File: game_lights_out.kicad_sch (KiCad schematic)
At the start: 94 parts, among them SW1 SW_MEC_5E, SW10 SW_MEC_5E, SW11 SW_MEC_5E, SW12 SW_MEC_5E, SW13 SW_MEC_5E, SW14 SW_MEC_5E, SW15 SW_MEC_5E, SW16 SW_MEC_5E, SW17 SW_MEC_5E, SW18 SW_MEC_5E, SW19 SW_MEC_5E, SW2 SW_MEC_5E, SW20 SW_MEC_5E, SW21 SW_MEC_5E, SW22 SW_MEC_5E, SW23 SW_MEC_5E, SW24 SW_MEC_5E, SW25 SW_MEC_5E, SW26 SW_MEC_5E, SW27 SW_MEC_5E, SW28 SW_MEC_5E, SW29 SW_MEC_5E, SW3 SW_MEC_5E, SW30 SW_MEC_5E, SW31 SW_MEC_5E, SW32 SW_MEC_5E, SW33 SW_MEC_5E, SW34 SW_MEC_5E, SW35 SW_MEC_5E, SW36 SW_MEC_5E, SW37 SW_MEC_5E, SW38 SW_MEC_5E, SW39 SW_MEC_5E, SW4 SW_MEC_5E, SW40 SW_MEC_5E, SW5 SW_MEC_5E, SW6 SW_MEC_5E, SW7 SW_MEC_5E, SW8 SW_MEC_5E, SW9 SW_MEC_5E, U1 ATmega328-P, U2 ULN2803A

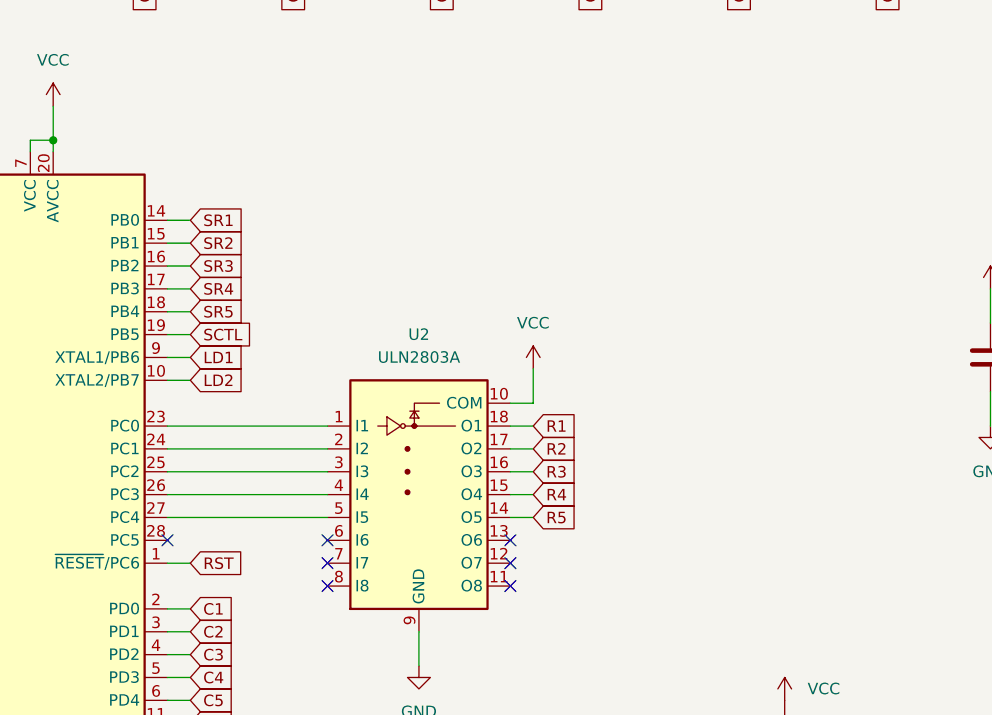
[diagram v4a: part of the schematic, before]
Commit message: Added speaker
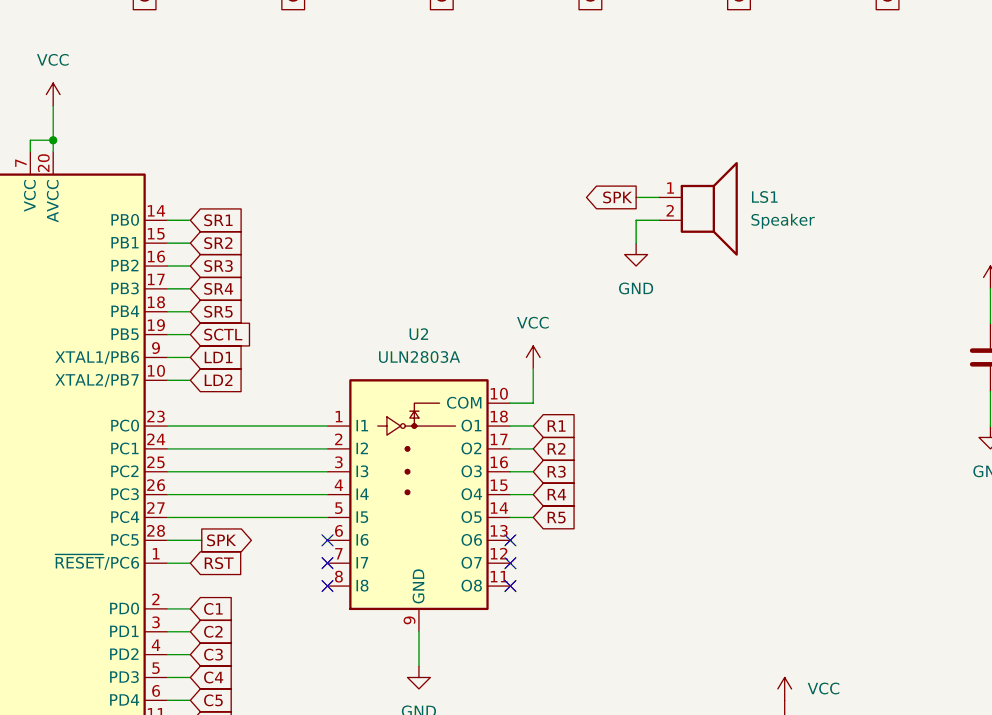
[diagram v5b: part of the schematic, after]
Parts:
- added LS1: Speaker, Connector_PinHeader_2.54mm:PinHeader_1x02_P2.54mm_Vertical, symbol Device:Speaker
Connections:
- net GND: now also LS1.2
- net SPK: now reaches U1.28 (PC5)
- net SPK: now also LS1.1
- no-connect marks 49 -> 48
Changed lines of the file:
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@@
   (junction (at 176.53 55.88) (diameter 0) (color 0 0 0 0)
   )
-  (no_connect (at 50.8 152.4))
   (no_connect (at 99.06 85.09))
   (no_connect (at 82.55 85.09))
@@
     (stroke (width 0) (type default))
   )
+  (wire (pts (xy 102.87 116.84) (xy 105.41 116.84))
+    (stroke (width 0) (type default))
+  )
   (wire (pts (xy 92.71 78.74) (xy 92.71 82.55))
     (stroke (width 0) (type default))
@@
     (stroke (width 0) (type default))
   )
+  (wire (pts (xy 50.8 152.4) (xy 54.61 152.4))
+    (stroke (width 0) (type default))
+  )
   (wire (pts (xy 13.97 40.64) (xy 13.97 54.61))
     (stroke (width 0) (type default))
@@
     (stroke (width 0) (type default))
   )
+  (wire (pts (xy 102.87 114.3) (xy 105.41 114.3))
+    (stroke (width 0) (type default))
+  )
   (wire (pts (xy 266.7 83.82) (xy 266.7 88.9))
     (stroke (width 0) (type default))
@@
     (stroke (width 0) (type default))
   )
+  (wire (pts (xy 102.87 119.38) (xy 102.87 116.84))
+    (stroke (width 0) (type default))
+  )
   (wire (pts (xy 41.91 36.83) (xy 59.69 36.83))
     (stroke (width 0) (type default))
@@
     )
   )
+  (global_label "SPK" (shape output) (at 54.61 152.4 0) (fields_autoplaced)
+    (effects (font (size 1.27 1.27)) (justify left))
+    (property "Intersheetrefs" "${INTERSHEET_REFS}" (at 61.3447 152.4 0)
+      (effects (font (size 1.27 1.27)) (justify left) hide)
+    )
+  )
   (global_label "SR3" (shape input) (at 53.34 121.92 0) (fields_autoplaced)
     (effects (font (size 1.27 1.27)) (justify left))
@@
     )
   )
+  (global_label "SPK" (shape output) (at 102.87 114.3 180) (fields_autoplaced)
+    (effects (font (size 1.27 1.27)) (justify right))
+    (property "Intersheetrefs" "${INTERSHEET_REFS}" (at 96.1353 114.3 0)
+      (effects (font (size 1.27 1.27)) (justify right) hide)
+    )
+  )
   (global_label "C3" (shape input) (at 53.34 165.1 0) (fields_autoplaced)
     (effects (font (size 1.27 1.27)) (justify left))
@@
     )
   )
+  (symbol (lib_id "Device:Speaker") (at 110.49 114.3 0) (unit 1)
+    (in_bom yes) (on_board yes) (dnp no) (fields_autoplaced)
+    (property "Reference" "LS1" (at 115.57 114.3 0)
+      (effects (font (size 1.27 1.27)) (justify left))
+    )
+    (property "Value" "Speaker" (at 115.57 116.84 0)
+      (effects (font (size 1.27 1.27)) (justify left))
+    )
+    (property "Footprint" "Connector_PinHeader_2.54mm:PinHeader_1x02_P2.54mm_Vertical" (at 110.49 119.38 0)
+      (effects (font (size 1.27 1.27)) hide)
+    )
+    (property "Datasheet" "~" (at 110.236 115.57 0)
+      (effects (font (size 1.27 1.27)) hide)
+    )
+    (pin "1")
+    (pin "2")
+    (instances
+      (project "game_lights_out"
+        (path "/ccb92925-3037-4924-9354-2881b1b404a5"
+          (reference "LS1") (unit 1)
+        )
+      )
+    )
+  )
   (symbol (lib_id "power:VCC") (at 91.44 133.35 0) (unit 1)
     (in_bom yes) (on_board yes) (dnp no) (fields_autoplaced)
@@
         )
       )
+    )
+  )
+  (symbol (lib_id "power:GND") (at 102.87 119.38 0) (unit 1)
+    (in_bom yes) (on_board yes) (dnp no) (fields_autoplaced)
+    (property "Reference" "#PWR05" (at 102.87 125.73 0)
+      (effects (font (size 1.27 1.27)) hide)
+    )
+    (property "Value" "GND" (at 102.87 124.46 0)
+      (effects (font (size 1.27 1.27)))
+    )
+    (property "Footprint" "" (at 102.87 119.38 0)
+      (effects (font (size 1.27 1.27)) hide)
+    )
+    (property "Datasheet" "" (at 102.87 119.38 0)
+      (effects (font (size 1.27 1.27)) hide)
+    )
+    (pin "1")
+    (instances
+      (project "game_lights_out"
+        (path "/ccb92925-3037-4924-9354-2881b1b404a5"
+          (reference "#PWR05") (unit 1)
+        )
+      )

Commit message: Board clean up - Remove mounting holes - Remove component outlines - Remove matrix outline - Add SMD pads for power
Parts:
- removed H1, H2, H3, H4: MountingHole_Pad, MountingHole:MountingHole_2.5mm_Pad, symbol Mechanical:MountingHole_Pad
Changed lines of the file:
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@@
-    )
-  )
-  (symbol (lib_id "power:VCC") (at 143.51 170.18 0) (unit 1)
-    (in_bom yes) (on_board yes) (dnp no) (fields_autoplaced)
-    (property "Reference" "#PWR02" (at 143.51 173.99 0)
-      (effects (font (size 1.27 1.27)) hide)
-    )
-    (property "Value" "VCC" (at 146.05 168.9099 0)
-      (effects (font (size 1.27 1.27)) (justify left))
-    )
-    (property "Footprint" "" (at 143.51 170.18 0)
-      (effects (font (size 1.27 1.27)) hide)
-    )
-    (property "Datasheet" "" (at 143.51 170.18 0)
-      (effects (font (size 1.27 1.27)) hide)
-    )
-    (pin "1")
-    (instances
-      (project "game_lights_out"
-        (path "/ccb92925-3037-4924-9354-2881b1b404a5"
-          (reference "#PWR02") (unit 1)
-        )
-      )
     )
   )
@@
     )
   )
-  (symbol (lib_id "Mechanical:MountingHole_Pad") (at 143.51 187.96 0) (unit 1)
-    (in_bom yes) (on_board yes) (dnp no) (fields_autoplaced)
-    (property "Reference" "H2" (at 146.05 185.42 0)
-      (effects (font (size 1.27 1.27)) (justify left))
-    )
-    (property "Value" "MountingHole_Pad" (at 146.05 187.96 0)
-      (effects (font (size 1.27 1.27)) (justify left))
-    )
-    (property "Footprint" "MountingHole:MountingHole_2.5mm_Pad" (at 143.51 187.96 0)
-      (effects (font (size 1.27 1.27)) hide)
-    )
-    (property "Datasheet" "~" (at 143.51 187.96 0)
-      (effects (font (size 1.27 1.27)) hide)
-    )
-    (pin "1")
-    (instances
-      (project "game_lights_out"
-        (path "/ccb92925-3037-4924-9354-2881b1b404a5"
-          (reference "H2") (unit 1)
-        )
-      )
-    )
-  )
-  (symbol (lib_id "power:GND") (at 143.51 190.5 0) (unit 1)
-    (in_bom yes) (on_board yes) (dnp no) (fields_autoplaced)
-    (property "Reference" "#PWR04" (at 143.51 196.85 0)
-      (effects (font (size 1.27 1.27)) hide)
-    )
-    (property "Value" "GND" (at 143.51 195.58 0)
-      (effects (font (size 1.27 1.27)))
-    )
-    (property "Footprint" "" (at 143.51 190.5 0)
-      (effects (font (size 1.27 1.27)) hide)
-    )
-    (property "Datasheet" "" (at 143.51 190.5 0)
-      (effects (font (size 1.27 1.27)) hide)
-    )
-    (pin "1")
-    (instances
-      (project "game_lights_out"
-        (path "/ccb92925-3037-4924-9354-2881b1b404a5"
-          (reference "#PWR04") (unit 1)
-        )
-      )
-    )
-  )
   (symbol (lib_id "LED:CQY99") (at 241.3 53.34 270) (unit 1)
     (in_bom yes) (on_board yes) (dnp no) (fields_autoplaced)
@@
     )
   )
-  (symbol (lib_id "power:VCC") (at 119.38 170.18 0) (unit 1)
-    (in_bom yes) (on_board yes) (dnp no) (fields_autoplaced)
-    (property "Reference" "#PWR01" (at 119.38 173.99 0)
-      (effects (font (size 1.27 1.27)) hide)
-    )
-    (property "Value" "VCC" (at 121.92 168.9099 0)
-      (effects (font (size 1.27 1.27)) (justify left))
-    )
-    (property "Footprint" "" (at 119.38 170.18 0)
-      (effects (font (size 1.27 1.27)) hide)
-    )
-    (property "Datasheet" "" (at 119.38 170.18 0)
-      (effects (font (size 1.27 1.27)) hide)
-    )
-    (pin "1")
-    (instances
-      (project "game_lights_out"
-        (path "/ccb92925-3037-4924-9354-2881b1b404a5"
-          (reference "#PWR01") (unit 1)
-        )
-      )
-    )
-  )
   (symbol (lib_id "Switch:SW_MEC_5E") (at 54.61 71.12 0) (unit 1)
     (in_bom yes) (on_board yes) (dnp no) (fields_autoplaced)
@@
         (path "/ccb92925-3037-4924-9354-2881b1b404a5"
           (reference "D27") (unit 1)
-        )
-      )
-    )
-  )
-  (symbol (lib_id "Mechanical:MountingHole_Pad") (at 143.51 172.72 180) (unit 1)
-    (in_bom yes) (on_board yes) (dnp no) (fields_autoplaced)
-    (property "Reference" "H4" (at 146.05 172.72 0)
-      (effects (font (size 1.27 1.27)) (justify right))
-    )
-    (property "Value" "MountingHole_Pad" (at 146.05 175.26 0)
-      (effects (font (size 1.27 1.27)) (justify right))
-    )
-    (property "Footprint" "MountingHole:MountingHole_2.5mm_Pad" (at 143.51 172.72 0)
-      (effects (font (size 1.27 1.27)) hide)
-    )
-    (property "Datasheet" "~" (at 143.51 172.72 0)
-      (effects (font (size 1.27 1.27)) hide)
-    )
-    (pin "1")
-    (instances
-      (project "game_lights_out"
-        (path "/ccb92925-3037-4924-9354-2881b1b404a5"
-          (reference "H4") (unit 1)
         )
       )
@@
     )
   )
-  (symbol (lib_id "Mechanical:MountingHole_Pad") (at 119.38 187.96 0) (unit 1)
-    (in_bom yes) (on_board yes) (dnp no) (fields_autoplaced)
-    (property "Reference" "H1" (at 121.92 185.42 0)
-      (effects (font (size 1.27 1.27)) (justify left))
-    )
-    (property "Value" "MountingHole_Pad" (at 121.92 187.96 0)
-      (effects (font (size 1.27 1.27)) (justify left))
-    )
-    (property "Footprint" "MountingHole:MountingHole_2.5mm_Pad" (at 119.38 187.96 0)
-      (effects (font (size 1.27 1.27)) hide)
-    )
-    (property "Datasheet" "~" (at 119.38 187.96 0)
-      (effects (font (size 1.27 1.27)) hide)
-    )
-    (pin "1")
-    (instances
-      (project "game_lights_out"
-        (path "/ccb92925-3037-4924-9354-2881b1b404a5"
-          (reference "H1") (unit 1)
-        )
-      )
-    )
-  )
   (symbol (lib_id "Switch:SW_MEC_5E") (at 36.83 71.12 0) (unit 1)
     (in_bom yes) (on_board yes) (dnp no) (fields_autoplaced)
@@
     )
   )
-  (symbol (lib_id "power:GND") (at 119.38 190.5 0) (unit 1)
-    (in_bom yes) (on_board yes) (dnp no) (fields_autoplaced)
-    (property "Reference" "#PWR03" (at 119.38 196.85 0)
-      (effects (font (size 1.27 1.27)) hide)
-    )
-    (property "Value" "GND" (at 119.38 195.58 0)
-      (effects (font (size 1.27 1.27)))
-    )
-    (property "Footprint" "" (at 119.38 190.5 0)
-      (effects (font (size 1.27 1.27)) hide)
-    )
-    (property "Datasheet" "" (at 119.38 190.5 0)
-      (effects (font (size 1.27 1.27)) hide)
-    )
-    (pin "1")
-    (instances
-      (project "game_lights_out"
-        (path "/ccb92925-3037-4924-9354-2881b1b404a5"
-          (reference "#PWR03") (unit 1)
-        )
-      )
-    )
-  )
   (symbol (lib_id "Switch:SW_MEC_5E") (at 54.61 29.21 0) (unit 1)
     (in_bom yes) (on_board yes) (dnp no) (fields_autoplaced)
@@
         )
       )
-    )
-  )
-  (symbol (lib_id "Mechanical:MountingHole_Pad") (at 119.38 172.72 180) (unit 1)
-    (in_bom yes) (on_board yes) (dnp no) (fields_autoplaced)
-    (property "Reference" "H3" (at 121.92 172.72 0)
-      (effects (font (size 1.27 1.27)) (justify right))
-    )
-    (property "Value" "MountingHole_Pad" (at 121.92 175.26 0)
-      (effects (font (size 1.27 1.27)) (justify right))
-    )
-    (property "Footprint" "MountingHole:MountingHole_2.5mm_Pad" (at 119.38 172.72 0)
-      (effects (font (size 1.27 1.27)) hide)
-    )
-    (property "Datasheet" "~" (at 119.38 172.72 0)
-      (effects (font (size 1.27 1.27)) hide)
-    )
-    (pin "1")
-    (instances
-      (project "game_lights_out"
-        (path "/ccb92925-3037-4924-9354-2881b1b404a5"
-          (reference "H3") (unit 1)
-        )
-      )

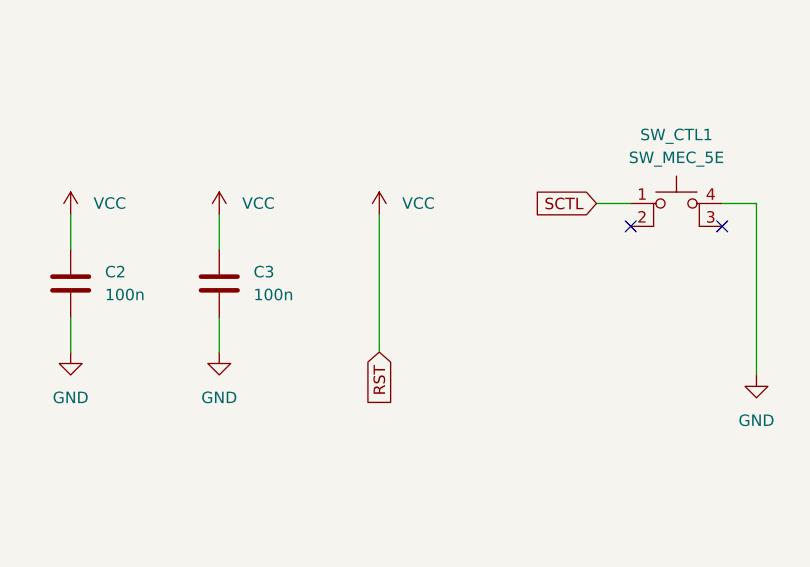
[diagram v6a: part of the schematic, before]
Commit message: Added reset pull up resitor
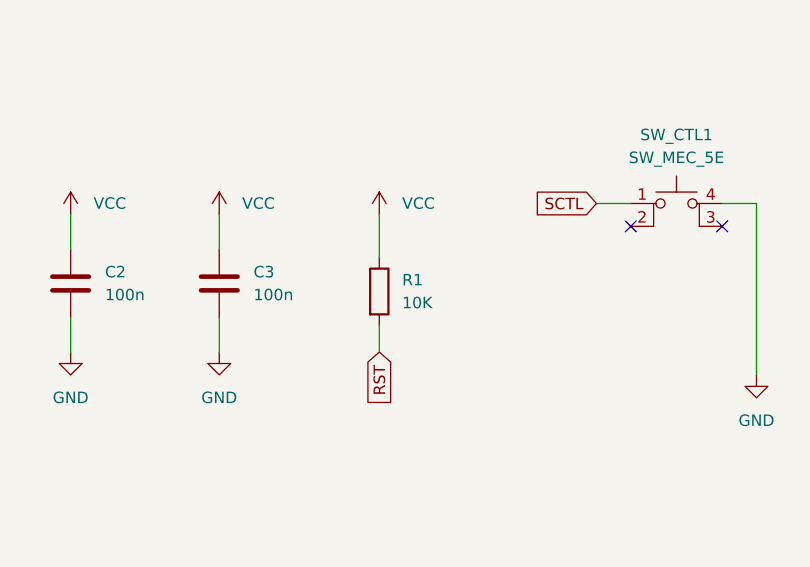
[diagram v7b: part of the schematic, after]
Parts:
- added R1: 10K, Resistor_THT:R_Axial_DIN0207_L6.3mm_D2.5mm_P7.62mm_Horizontal, symbol Device:R
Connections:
- net VCC: now also R1.1; no longer U1.1 (~{RESET}/PC6)
- new net RST: R1.2, U1.1 (~{RESET}/PC6)
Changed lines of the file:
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@@
+    (stroke (width 0) (type default))
+  )
+  (wire (pts (xy 194.31 129.159) (xy 194.31 124.46))
     (stroke (width 0) (type default))
   )
@@
     (stroke (width 0) (type default))
   )
-  (wire (pts (xy 194.31 124.46) (xy 194.31 139.7))
-    (stroke (width 0) (type default))
-  )
   (wire (pts (xy 91.44 144.78) (xy 88.9 144.78))
     (stroke (width 0) (type default))
@@
   )
   (wire (pts (xy 91.44 137.16) (xy 91.44 133.35))
+    (stroke (width 0) (type default))
+  )
+  (wire (pts (xy 194.31 136.779) (xy 194.31 139.7))
     (stroke (width 0) (type default))
   )
@@
         )
       )
+    )
+  )
+  (symbol (lib_id "Device:R") (at 194.31 132.969 0) (unit 1)
+    (in_bom yes) (on_board yes) (dnp no) (fields_autoplaced)
+    (property "Reference" "R1" (at 196.85 131.699 0)
+      (effects (font (size 1.27 1.27)) (justify left))
+    )
+    (property "Value" "10K" (at 196.85 134.239 0)
+      (effects (font (size 1.27 1.27)) (justify left))
+    )
+    (property "Footprint" "Resistor_THT:R_Axial_DIN0207_L6.3mm_D2.5mm_P7.62mm_Horizontal" (at 192.532 132.969 90)
+      (effects (font (size 1.27 1.27)) hide)
+    )
+    (property "Datasheet" "~" (at 194.31 132.969 0)
+      (effects (font (size 1.27 1.27)) hide)
+    )
+    (pin "1")
+    (pin "2")
+    (instances
+      (project "game_lights_out"
+        (path "/ccb92925-3037-4924-9354-2881b1b404a5"
+          (reference "R1") (unit 1)
+        )
+      )
